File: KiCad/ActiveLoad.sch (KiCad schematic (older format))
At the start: 61 parts, among them J1 AuxPower, J2 TWI, J3 PDI, J4 TC74X-3.3, J5 PowerInput, J6 FAN, Q2 BC817, Q3 BD911, Q4 BD136, SW1 SW_SPDT, SW2 SW_SPDT, U1 UA78M33, U2 L78M12, U3 ATXMEGA32E5-AU, U4 LM358, U5 TL081

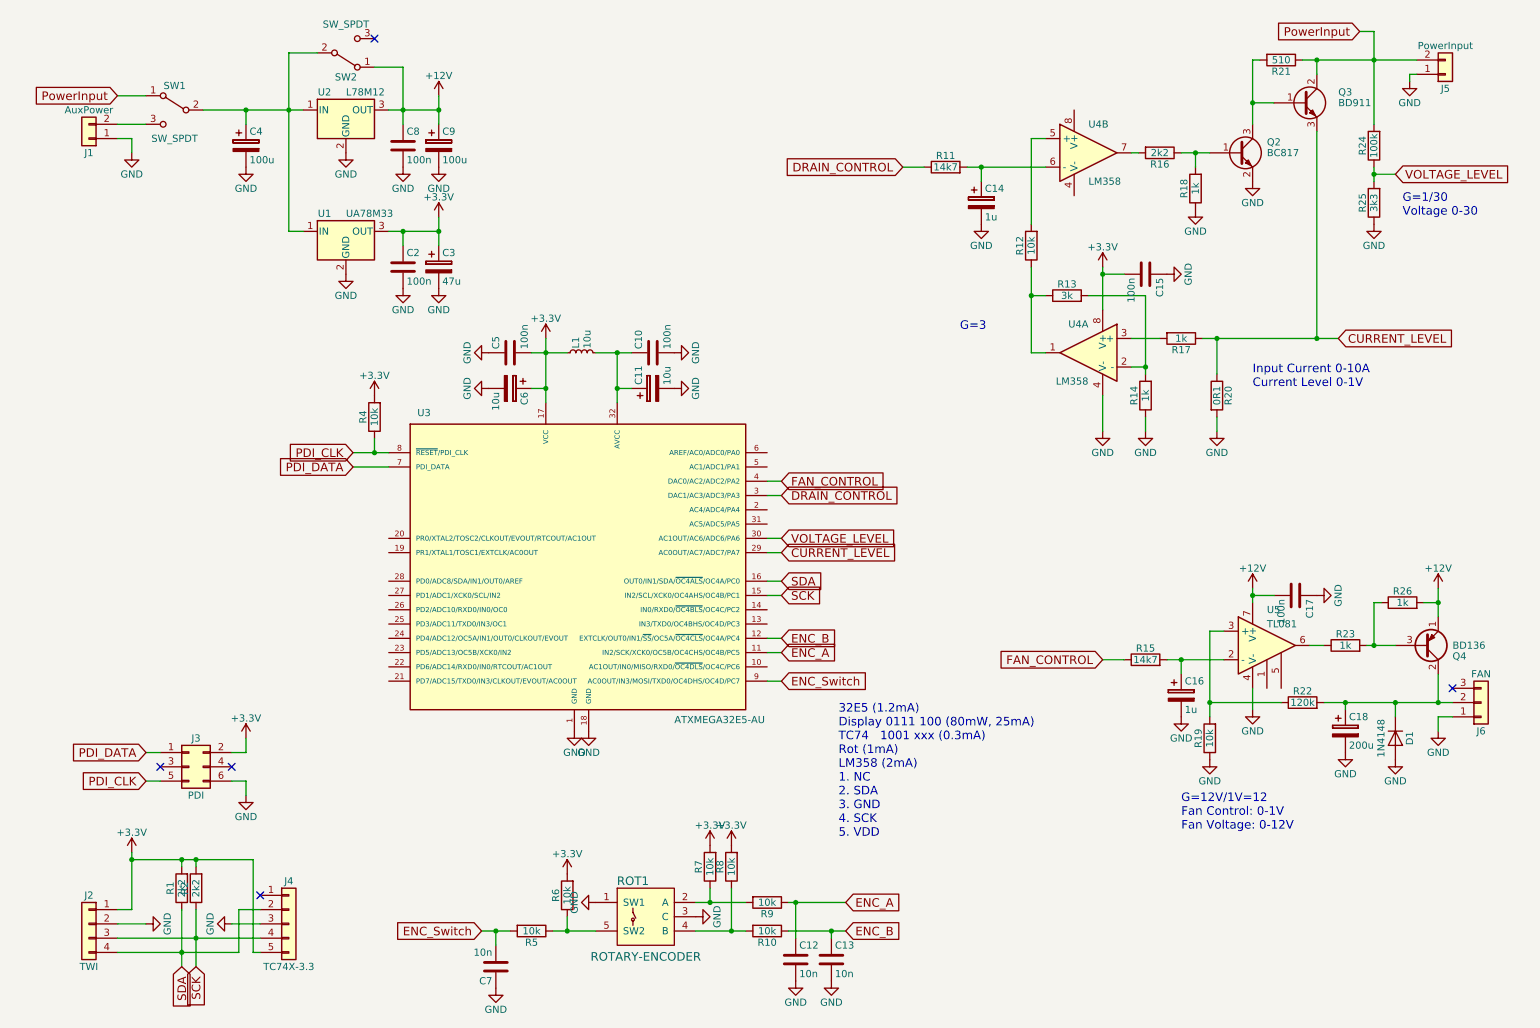
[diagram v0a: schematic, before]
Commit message: Diodes around 7812 added
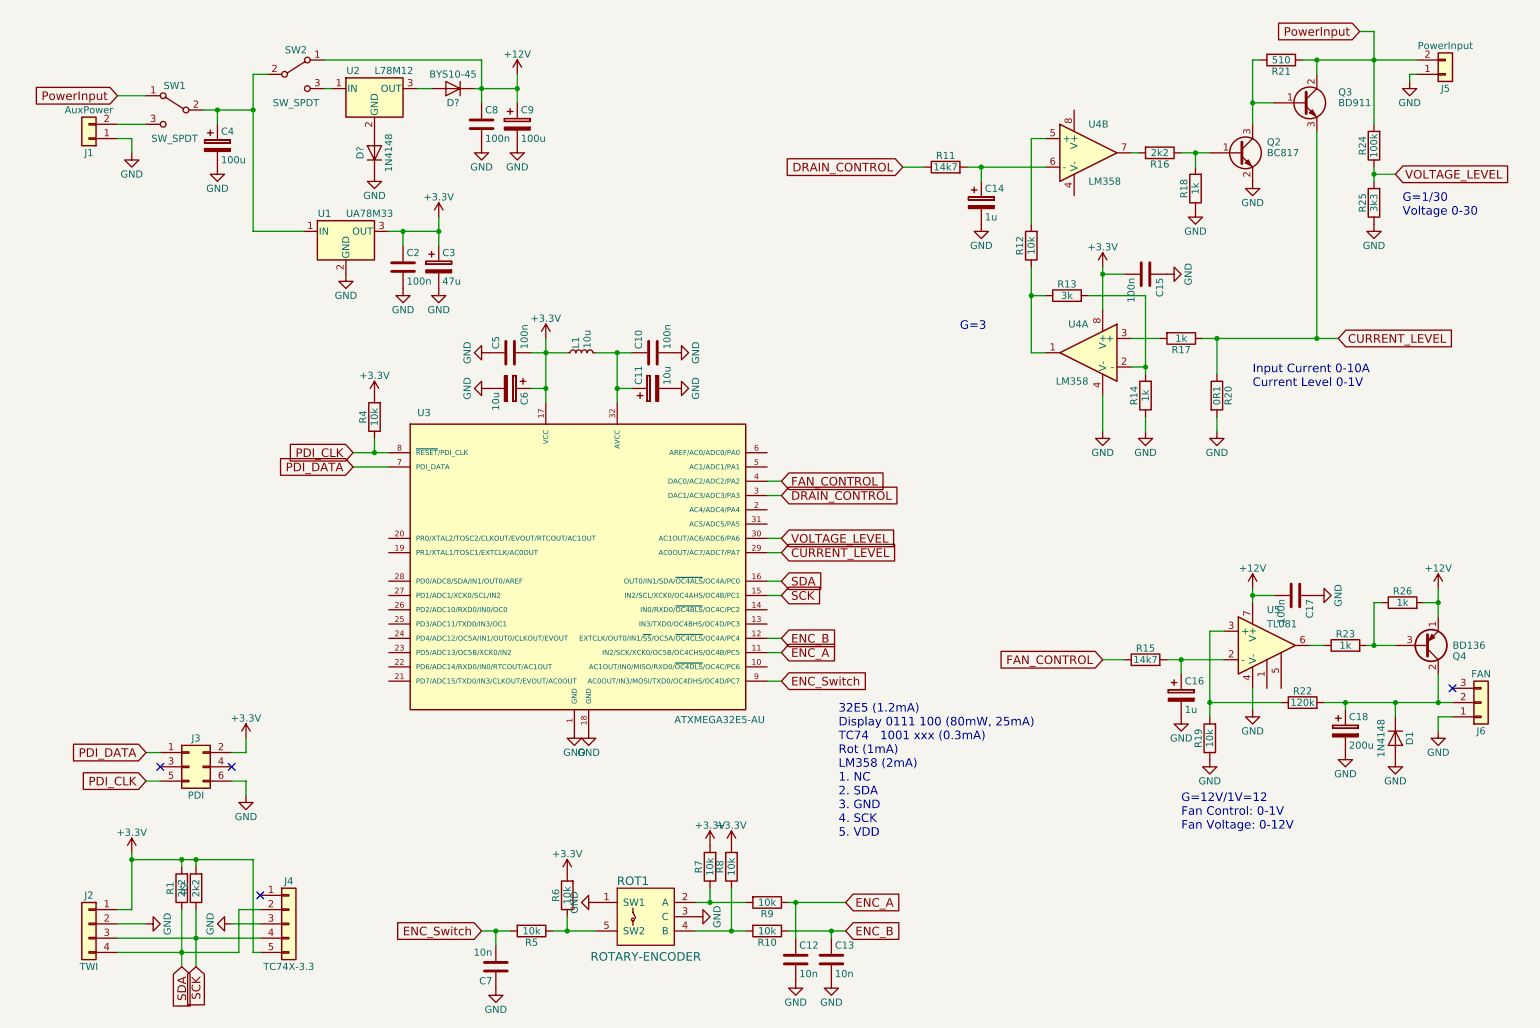
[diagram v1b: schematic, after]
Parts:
- added D?: 1N4148, Diodes_SMD:D_1206, symbol D
- added D?: BYS10-45, Diodes_SMD:D_1206, symbol D
- R20: footprint Resistors_THT:R_Axial_Power_L48.0mm_W12.5mm_P55.88mm -> JPResistors:R_Axial_Power_L48.0mm_W12.5mm_P50.8mm
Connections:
- net +12V: now also D?.1 (K); no longer U2.3 (OUT)
- net GND: now also D?.1 (K); no longer U2.2 (GND)
- net at C4.1, SW1.2 (B), SW2.2 (B)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: no longer U2.1 (IN)
- net at SW2.3 (C): now also U2.1 (IN)
- new net: D?.2 (A), U2.2 (GND)
- new net: D?.2 (A), U2.3 (OUT)
- no-connect marks 5 -> 4
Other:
- moved on the sheet: C4, C8, C9, SW2, U2

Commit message: Finishing touches
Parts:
- D3: renamed from D?; footprint Diodes_SMD:D_1206 -> Diodes_SMD:D_SMA
- J2: value TWI -> OLED I2C; footprint Pin_Headers:Pin_Header_Straight_1x04_Pitch2.54mm -> JPDisplays:OLED_0.96inch_128x64_I2C
- gave numbers to parts that had none: 1
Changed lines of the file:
@@
 P 1100 7100
 F 0 "J2" H 1100 7300 50  0000 C CNN
-F 1 "TWI" H 1100 6800 50  0000 C CNN
-F 2 "Pin_Headers:Pin_Header_Straight_1x04_Pitch2.54mm" H 1100 7100 50  0001 C CNN
+F 1 "OLED I2C" H 1100 6800 50  0000 C CNN
+F 2 "JPDisplays:OLED_0.96inch_128x64_I2C" H 1100 7100 50  0001 C CNN
 F 3 "" H 1100 7100 50  0001 C CNN
 	1    1100 7100
@@
 	8400 3000 8600 3000
 Wire Wire Line
-	8900 3000 9000 3000
-Wire Wire Line
-	9000 3000 9700 3000
-Wire Wire Line
-	9700 3000 9850 3000
+	8900 3000 9850 3000
 Wire Wire Line
 	9000 3000 9000 3250
@@
 	8400 3200 8500 3200
 Wire Wire Line
-	8500 2700 8500 3200
-Wire Wire Line
-	8500 3200 8500 3250
+	8500 2700 8500 3250
 Wire Wire Line
 	8500 2700 8100 2700
@@
 	7800 2700 7700 2700
 Wire Wire Line
-	7700 2500 7700 2700
-Wire Wire Line
-	7700 2700 7700 3100
+	7700 2500 7700 3100
 Wire Wire Line
 	7700 3100 7800 3100
@@
 	8200 3650 8200 3400
 Wire Wire Line
-	8200 2500 8200 2550
-Wire Wire Line
-	8200 2550 8200 2800
+	8200 2500 8200 2800
 Wire Wire Line
 	8350 2550 8200 2550
@@
 	8400 1700 8450 1700
 Wire Wire Line
-	8750 1700 8850 1700
-Wire Wire Line
-	8850 1700 8950 1700
+	8750 1700 8950 1700
 Wire Wire Line
 	8850 1800 8850 1700
 Connection ~ 8850 1700
 Wire Wire Line
-	9250 1050 9250 1350
-Wire Wire Line
-	9250 1350 9250 1500
+	9250 1050 9250 1500
 Wire Wire Line
 	9250 1050 9300 1050
@@
 Connection ~ 9250 1350
 Wire Wire Line
-	9600 1050 9700 1050
-Wire Wire Line
-	9700 1050 10100 1050
-Wire Wire Line
-	10100 1050 10400 1050
+	9600 1050 10400 1050
 Wire Wire Line
 	9700 1050 9700 1150
@@
 	9700 3000 9700 1550
 Wire Wire Line
-	4300 3000 4300 3100
-Wire Wire Line
-	4300 3100 4300 3350
-Wire Wire Line
-	4300 3350 4300 3450
-Wire Wire Line
-	4200 3100 4300 3100
-Wire Wire Line
-	4300 3100 4450 3100
+	4300 3000 4300 3450
+Wire Wire Line
+	4200 3100 4450 3100
 Connection ~ 4300 3100
 Wire Wire Line
-	4650 3100 4800 3100
-Wire Wire Line
-	4800 3100 4900 3100
-Wire Wire Line
-	4800 3100 4800 3350
-Wire Wire Line
-	4800 3350 4800 3450
+	4650 3100 4900 3100
+Wire Wire Line
+	4800 3100 4800 3450
 Wire Wire Line
 	4900 3350 4800 3350
@@
 	3100 3700 3100 3800
 Wire Wire Line
-	2950 3800 3100 3800
-Wire Wire Line
-	3100 3800 3200 3800
+	2950 3800 3200 3800
 Wire Wire Line
 	3200 3900 2950 3900
@@
 Connection ~ 9700 3000
 Wire Wire Line
-	10100 1800 10100 1850
-Wire Wire Line
-	10100 1850 10100 1900
-Wire Wire Line
-	10100 850  10100 1050
-Wire Wire Line
-	10100 1050 10100 1500
+	10100 1800 10100 1900
+Wire Wire Line
+	10100 850  10100 1500
 Connection ~ 10100 1050
 Connection ~ 10100 1850
 Wire Wire Line
-	1300 7300 1750 7300
-Wire Wire Line
-	1750 7300 2150 7300
-Wire Wire Line
-	1300 7200 1850 7200
-Wire Wire Line
-	1850 7200 2300 7200
+	1300 7300 2150 7300
+Wire Wire Line
+	1300 7200 2300 7200
 Wire Wire Line
 	1300 7100 1500 7100
@@
 	1400 7000 1300 7000
 Wire Wire Line
-	1400 6600 1400 6650
-Wire Wire Line
-	1400 6650 1400 7000
-Wire Wire Line
-	1750 7000 1750 7300
-Wire Wire Line
-	1750 7300 1750 7400
+	1400 6600 1400 7000
+Wire Wire Line
+	1750 7000 1750 7400
 Connection ~ 1750 7300
 Wire Wire Line
-	1850 7000 1850 7200
-Wire Wire Line
-	1850 7200 1850 7400
+	1850 7000 1850 7400
 Connection ~ 1850 7200
 Wire Wire Line
 	1850 6650 1850 6700
 Wire Wire Line
-	1400 6650 1750 6650
-Wire Wire Line
-	1750 6650 1850 6650
-Wire Wire Line
-	1850 6650 2250 6650
+	1400 6650 2250 6650
 Connection ~ 1400 6650
 Wire Wire Line
@@
 Connection ~ 1750 6650
 Wire Wire Line
-	10050 5150 10100 5150
-Wire Wire Line
-	10100 5150 10250 5150
+	10050 5150 10250 5150
 Wire Wire Line
 	10150 4850 10100 4850
@@
 Connection ~ 10100 5150
 Wire Wire Line
-	10550 4750 10550 4850
-Wire Wire Line
-	10550 4850 10550 4950
+	10550 4750 10550 4950
 Wire Wire Line
 	10450 4850 10550 4850
@@
 	10550 5550 10550 5350
 Wire Wire Line
-	9750 5550 9900 5550
-Wire Wire Line
-	9900 5550 10250 5550
-Wire Wire Line
-	10250 5550 10550 5550
-Wire Wire Line
-	10550 5550 10650 5550
+	9750 5550 10650 5550
 Wire Wire Line
 	10550 5750 10550 5650
@@
 	9450 5550 8950 5550
 Wire Wire Line
-	8950 5050 8950 5550
-Wire Wire Line
-	8950 5550 8950 5650
+	8950 5050 8950 5650
 Connection ~ 8950 5550
 Wire Wire Line
-	9250 4750 9250 4800
-Wire Wire Line
-	9250 4800 9250 4850
+	9250 4750 9250 4850
 Wire Wire Line
 	9400 4800 9250 4800
@@
 Connection ~ 9900 5550
 Wire Wire Line
-	8650 5250 8750 5250
-Wire Wire Line
-	8750 5250 9050 5250
+	8650 5250 9050 5250
 Wire Wire Line
 	8750 5250 8750 5350
@@
 	8350 5250 8200 5250
 Wire Wire Line
-	7250 1800 7350 1800
-Wire Wire Line
-	7350 1800 7800 1800
+	7250 1800 7800 1800
 Wire Wire Line
 	7350 1900 7350 1800
@@
 	3950 7250 3950 7150
 Wire Wire Line
-	3850 7150 3950 7150
-Wire Wire Line
-	3950 7150 4050 7150
+	3850 7150 4050 7150
 Connection ~ 3950 7150
 Wire Wire Line
-	5350 6950 5450 6950
-Wire Wire Line
-	5450 6950 5700 6950
-Wire Wire Line
-	5350 7150 5600 7150
-Wire Wire Line
-	5600 7150 5700 7150
+	5350 6950 5700 6950
+Wire Wire Line
+	5350 7150 5700 7150
 Wire Wire Line
 	5450 6850 5450 6950
@@
 Connection ~ 5600 7150
 Wire Wire Line
-	6000 6950 6050 6950
-Wire Wire Line
-	6050 6950 6400 6950
-Wire Wire Line
-	6000 7150 6300 7150
-Wire Wire Line
-	6300 7150 6400 7150
+	6000 6950 6400 6950
+Wire Wire Line
+	6000 7150 6400 7150
 Wire Wire Line
 	6050 7200 6050 6950
@@
 Connection ~ 6300 7150
 Wire Wire Line
-	3550 2150 3550 2250
-Wire Wire Line
-	3550 2250 3550 2350
+	3550 2150 3550 2350
 Wire Wire Line
 	3300 2350 3300 2250
@@
 	1300 1500 1500 1500
 Wire Wire Line
-	2250 1150 2250 1400
-Wire Wire Line
-	2250 1400 2250 2250
+	2250 1150 2250 2250
 Connection ~ 2250 1400
 Wire Wire Line
-	4100 1150 4100 1250
-Wire Wire Line
-	4100 1250 4100 1350
+	4100 1150 4100 1350
 Connection ~ 3850 1250
 Connection ~ 4100 1250
@@
 	8950 5050 9050 5050
 Wire Wire Line
-	3200 2250 3300 2250
-Wire Wire Line
-	3300 2250 3550 2250
+	3200 2250 3550 2250
 Connection ~ 2000 1400
 Wire Wire Line
 	2000 1500 2000 1400
 Wire Wire Line
-	1900 1400 2000 1400
-Wire Wire Line
-	2000 1400 2250 1400
+	1900 1400 2250 1400
 Wire Wire Line
 	2250 2250 2600 2250
@@
 Connection ~ 10250 5550
 Wire Wire Line
-	4350 7150 4450 7150
-Wire Wire Line
-	4450 7150 4650 7150
+	4350 7150 4650 7150
 Wire Wire Line
 	5850 5400 5950 5400
@@
 	2750 1050 3850 1050
 Wire Wire Line
-	3850 1050 3850 1250
-Wire Wire Line
-	3850 1250 3850 1350
-$Comp
-L D D?
+	3850 1050 3850 1350
+$Comp
+L D D2
 U 1 1 5AC556E6
 P 3100 1700
-F 0 "D?" H 3100 1800 50  0000 C CNN
+F 0 "D2" H 3100 1800 50  0000 C CNN
 F 1 "1N4148" H 3100 1600 50  0000 C CNN
 F 2 "Diodes_SMD:D_1206" H 3100 1700 50  0001 C CNN
@@
 $EndComp
 $Comp
-L D D?
+L D D3
 U 1 1 5AC55ED7
 P 3650 1250
-F 0 "D?" H 3650 1350 50  0000 C CNN
+F 0 "D3" H 3650 1350 50  0000 C CNN
 F 1 "BYS10-45" H 3650 1150 50  0000 C CNN
-F 2 "Diodes_SMD:D_1206" H 3650 1250 50  0001 C CNN
+F 2 "Diodes_SMD:D_SMA" H 3650 1250 50  0001 C CNN
 F 3 "" H 3650 1250 50  0001 C CNN
 	1    3650 1250
@@
 	3400 1250 3500 1250
 Wire Wire Line
-	3800 1250 3850 1250
-Wire Wire Line
-	3850 1250 4100 1250
+	3800 1250 4100 1250
 $EndSCHEMATC

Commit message: Finishing touches
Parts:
- C11, C6: footprint Capacitors_SMD:CP_Elec_4x5.8 -> Capacitors_SMD:CP_Elec_3x5.3
- D1, D2: footprint Diodes_SMD:D_1206 -> SMD_Packages:SMD-1206_Pol
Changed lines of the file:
@@
 F 0 "C6" H 4075 3450 50  0000 L CNN
 F 1 "10u" H 4075 3250 50  0000 L CNN
-F 2 "Capacitors_SMD:CP_Elec_4x5.8" H 4088 3200 50  0001 C CNN
+F 2 "Capacitors_SMD:CP_Elec_3x5.3" H 4088 3200 50  0001 C CNN
 F 3 "" H 4050 3350 50  0001 C CNN
 	1    4050 3350
@@
 F 0 "C11" H 5075 3450 50  0000 L CNN
 F 1 "10u" H 5075 3250 50  0000 L CNN
-F 2 "Capacitors_SMD:CP_Elec_4x5.8" H 5088 3200 50  0001 C CNN
+F 2 "Capacitors_SMD:CP_Elec_3x5.3" H 5088 3200 50  0001 C CNN
 F 3 "" H 5050 3350 50  0001 C CNN
 	1    5050 3350
@@
 F 0 "D1" H 10250 5900 50  0000 C CNN
 F 1 "1N4148" H 10250 5700 50  0000 C CNN
-F 2 "Diodes_SMD:D_1206" H 10250 5800 50  0001 C CNN
+F 2 "SMD_Packages:SMD-1206_Pol" H 10250 5800 50  0001 C CNN
 F 3 "" H 10250 5800 50  0001 C CNN
 	1    10250 5800
@@
 F 0 "D2" H 3100 1800 50  0000 C CNN
 F 1 "1N4148" H 3100 1600 50  0000 C CNN
-F 2 "Diodes_SMD:D_1206" H 3100 1700 50  0001 C CNN
+F 2 "SMD_Packages:SMD-1206_Pol" H 3100 1700 50  0001 C CNN
 F 3 "" H 3100 1700 50  0001 C CNN
 	1    3100 1700

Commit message: Brand new version
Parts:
- added D4: LED, Diodes_SMD:D_0805, symbol LED
- added R3: 3k3, Resistors_SMD:R_0805, symbol R
- Q4: value BD136 -> BD140
- R11, R15: value 14k7 -> 15k42
- R13: value 3k -> 3k3
- R21: value 510 -> 680
- U4: value LM358 -> OPA2170
- U5: value TL081 -> LM7321
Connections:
- net +12V: now also C15.2, R21.2, U4.8 (V+)
- net +3V3: now also D4.2 (A); no longer C15.2, U4.8 (V+)
- net GND: now also J6.3 (Pin_3), ROT1.5 (SW2); no longer J6.1 (Pin_1), ROT1.1 (SW1)
- net PowerInput: no longer R21.1
- net at Q2.3 (C), Q3.1 (B): now also R21.1; no longer R21.2
- net LED: now reaches U3.25 (PD3/ADC11/TXD0/IN3/OC1)
- net LED: now also R3.2
- net at R5.1, R6.1: now also ROT1.1 (SW1); no longer ROT1.5 (SW2)
- new net: D4.1 (K), R3.1
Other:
- note added: "Fan Control: 0-1V\nFan Voltage: 0-12V\nG=1V/12V=12\nR19/(R12+R22)=1/13"
- note added: "Max Voltage\nL78M12 - 35V\nUA78M33 - 25V\nOPA2170 - 36V\nLM7321 - 32V"
- note removed: "G=12V/1V=12\nFan Control: 0-1V\nFan Voltage: 0-12V"
- moved on the sheet: C16, C17, C18, C7, D1, J6, Q4, R15, R19, R21, R22, R23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

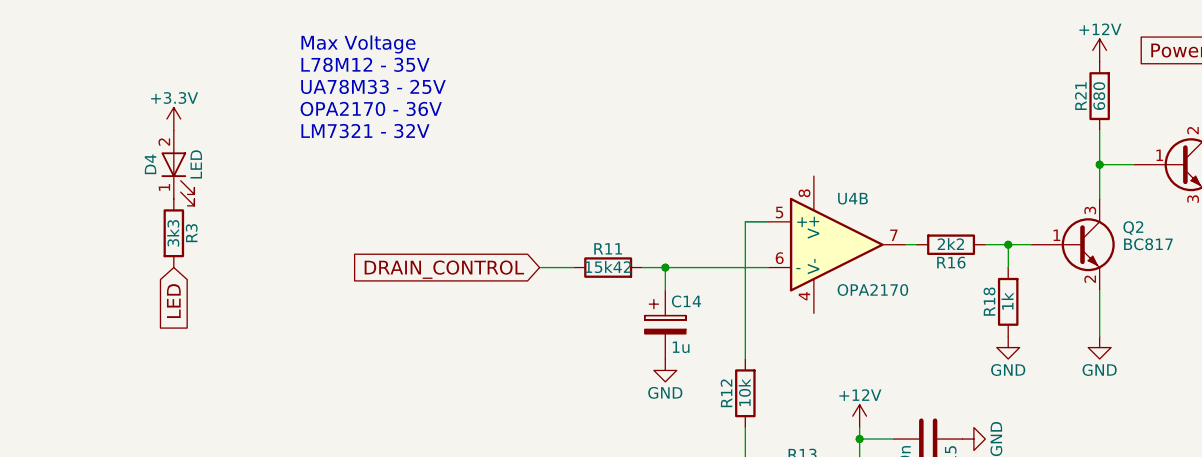
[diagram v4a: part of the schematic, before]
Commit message: Current metter added
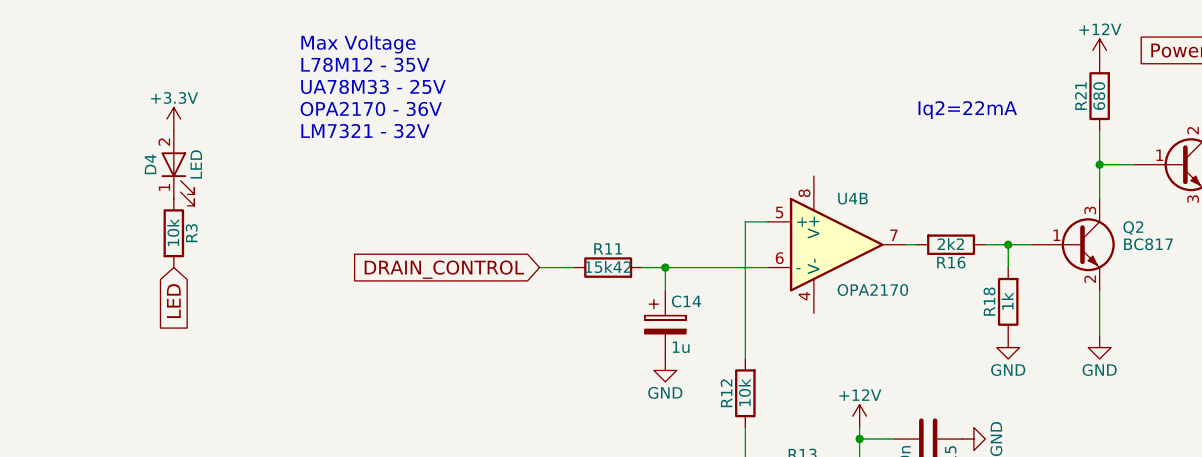
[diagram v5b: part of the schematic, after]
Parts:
- R3: value 3k3 -> 10k
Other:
- note added: "Iq2=22mA"
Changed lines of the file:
@@
 P 5200 1650
 F 0 "R3" V 5280 1650 50  0000 C CNN
-F 1 "3k3" V 5200 1650 50  0000 C CNN
+F 1 "10k" V 5200 1650 50  0000 C CNN
 F 2 "Resistors_SMD:R_0805" V 5130 1650 50  0001 C CNN
 F 3 "" H 5200 1650 50  0001 C CNN
@@
 Text Notes 5750 1250 0    60   ~ 0
 Max Voltage\nL78M12 - 35V\nUA78M33 - 25V\nOPA2170 - 36V\nLM7321 - 32V
+Text Notes 8450 1150 0    60   ~ 0
+Iq2=22mA
 $EndSCHEMATC

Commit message: Some fan control code
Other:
- note added: "Collector\nto case"
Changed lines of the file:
@@
 Text Notes 8450 1150 0    60   ~ 0
 Iq2=22mA
+Text Notes 9550 1150 0    60   ~ 0
+Collector\nto case
+Text Notes 10650 4900 0    60   ~ 0
+Collector\nto case
 $EndSCHEMATC
